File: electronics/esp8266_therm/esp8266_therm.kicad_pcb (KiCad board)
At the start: 2 copper layers, 40.6 x 45.7 mm, 20 parts, among them J1 CONN_01X02, J2 CONN_01X03, J3 CONN_01X03, J4 CONN_01X02, J5 CONN_01X08, J6 CONN_01X08, J7 CONN_01X02, J8 CONN_01X06, M1 BMP180_Breakout, Q1 Q_PMOS_GSD, SW1 SW_SPST, SW2 SW_SPST, U1 ESP-12E, U2 MCP1703A-3302/MB

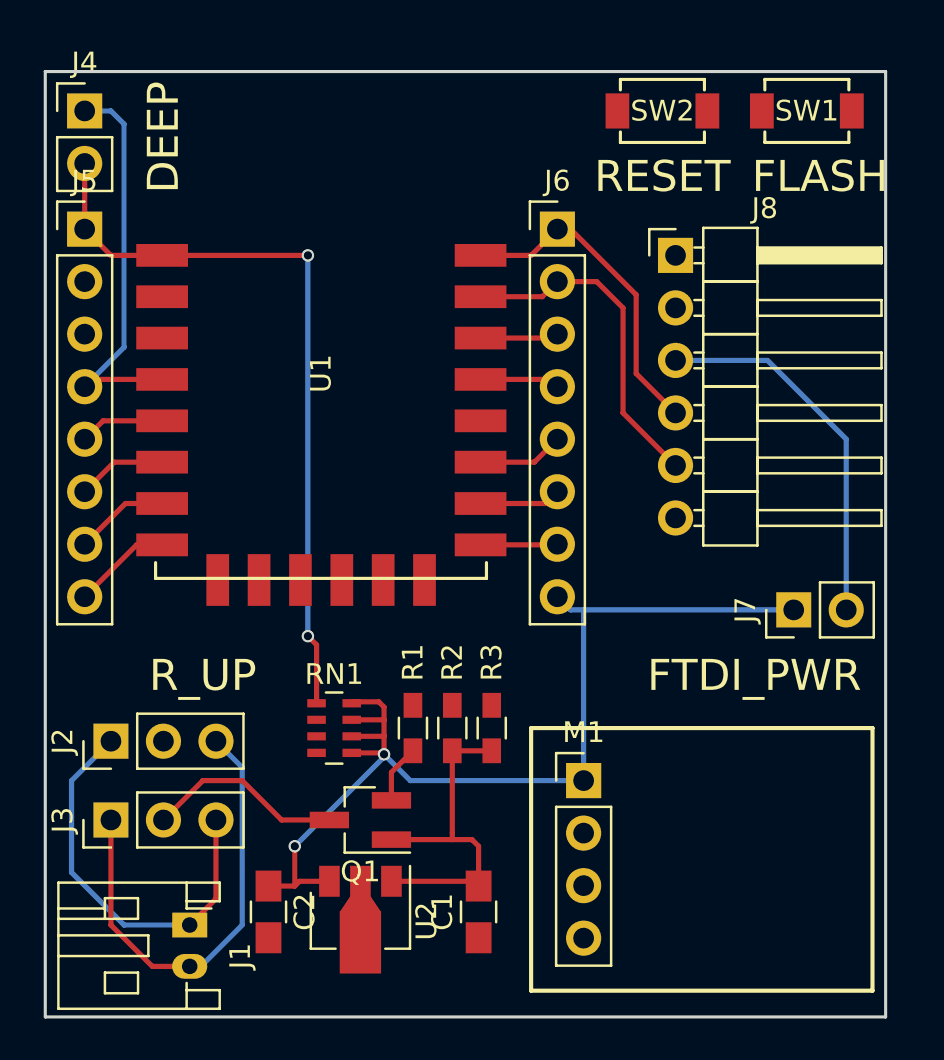
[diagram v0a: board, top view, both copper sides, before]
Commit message: Update pinout on board to match D1 mini
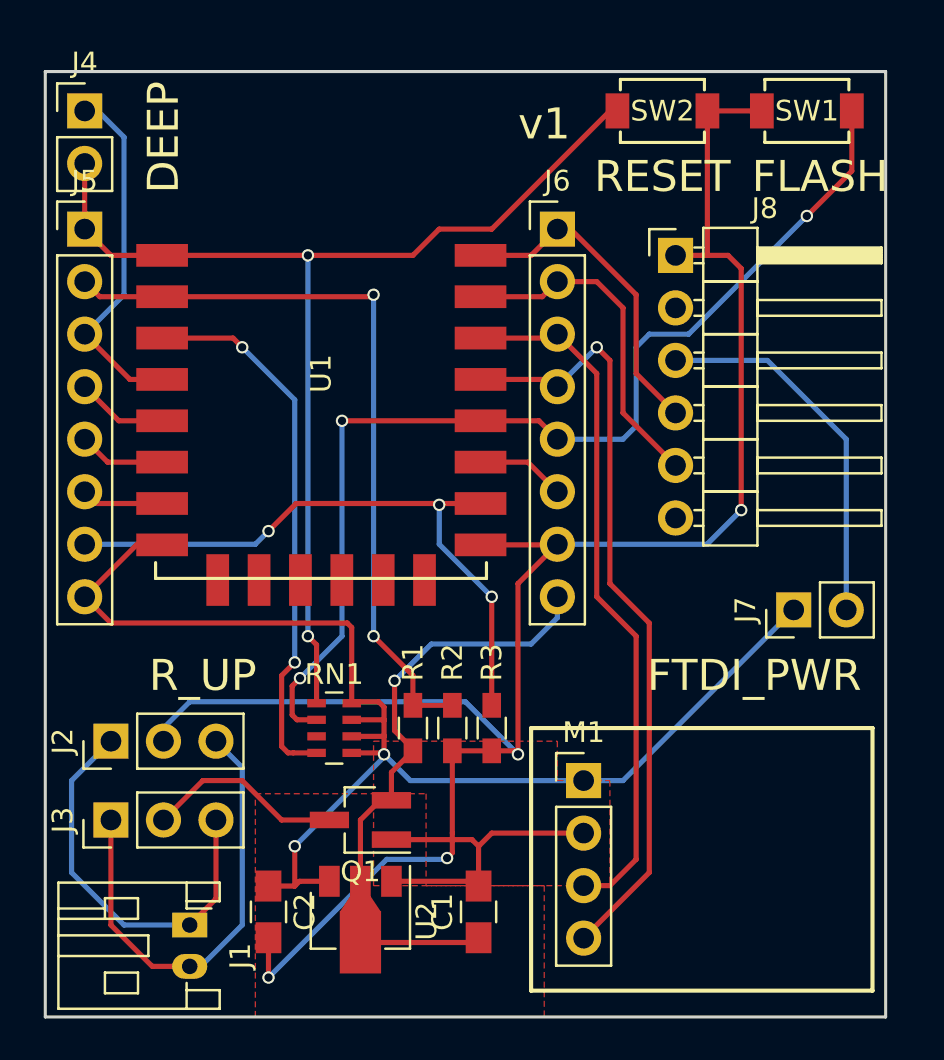
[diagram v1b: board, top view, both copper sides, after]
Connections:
- J5 pad 2: (no net) -> /ADC
- J5 pad 3: (no net) -> GPIO16
- J5 pad 4: GPIO16 -> /GPIO14
- J5 pad 5: /GPIO14 -> /GPIO12
- J5 pad 6: /GPIO12 -> /GPIO13
- J5 pad 7: /GPIO13 -> Net-(J5-Pad7)
- J6 pad 5: Net-(J6-Pad5) -> GPIO0
- J6 pad 8: +3V3 -> VBAT_PROT
- R3 pad 1: Net-(J6-Pad6) -> Net-(J5-Pad7)
- U1 pad 10: Net-(J6-Pad6) -> Net-(J5-Pad7)
- U1 pad 11: Net-(J6-Pad5) -> Net-(J6-Pad6)
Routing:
- net GND: track 21.7 -> 106.7 mm, vias 0 -> 4
- net GPIO0: track 0.00 -> 52.0 mm, vias 0 -> 3
- net /ADC: track 0.00 -> 36.9 mm, vias 0 -> 2
- net Net-(J6-Pad4): track 4.56 -> 38.7 mm, vias 0 -> 1
- net Net-(J5-Pad7): track 0.00 -> 30.2 mm, vias 0 -> 3
- net Net-(J6-Pad3): track 4.49 -> 34.5 mm
- net CH_PD: track 0.00 -> 25.8 mm, vias 0 -> 2
- net VBAT_PROT: track 3.89 -> 29.6 mm, vias 0 -> 1
- net RESET: track 36.3 -> 54.2 mm
- net +3V3: track 55.5 -> 66.4 mm
- net Net-(J6-Pad5): track 4.87 -> 0.00 mm
- net GPIO16: track 20.2 -> 18.1 mm
- net /GPIO14: track 4.81 -> 5.62 mm
- net /GPIO13: track 5.26 -> 4.68 mm
- added copper zone on F.Cu, net GND
- added copper zone on F.Cu, net VBAT_PROT
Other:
- board text added: "v1"
